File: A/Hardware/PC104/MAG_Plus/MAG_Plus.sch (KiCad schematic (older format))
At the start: 39 parts, among them J1 RPi_GPIO, J9 Conn_01x06_Male, SW1 SW_Push, U1 Payload, U12 PIC16F1847-I_SO, U13 LP38693MP-3.3, U14 LP38693MP-3.3, U15 LP38693MP-5.0, U16 LP38693MP-3.3, U2 ISO1540

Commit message: More PCB Changes
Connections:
- net PIC_3V3: no longer C6.1, R5.1, R6.1, U2.8 (VCC2)
- net PIC_3V3J: now also C6.1, R5.1, R6.1, U2.8 (VCC2)
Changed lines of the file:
@@
 PIC_SDA
 Text GLabel 2050 5200 1    50   Input ~ 0
-PIC_3V3
+PIC_3V3J
 $Comp
 L Device:R R6
@@
 PIC_SCL
 Text GLabel 2300 5200 1    50   Input ~ 0
-PIC_3V3
+PIC_3V3J
 Text GLabel 4900 4600 2    50   Input ~ 0
-PIC_3V3
+PIC_3V3J
 Text GLabel 4900 4800 2    50   Input ~ 0
 PIC_SCL
@@
 SAT_3V3
 Text GLabel 5750 5600 1    50   Input ~ 0
-PIC_3V3
+PIC_3V3J
 Text GLabel 5250 5900 3    50   Input ~ 0
 GND

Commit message: PCB update
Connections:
- net MAG_EN: now also J1.29 (GPIO05); no longer J1.15 (GPIO22)
- net FOD_DPL: now reaches J1.11 (GPIO17)
- new net FOD_CC: J1.15 (GPIO22)
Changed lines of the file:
@@
 Text GLabel 4500 6600 0    50   Input ~ 0
 FOD_EN
-Text GLabel 7600 2100 0    50   Input ~ 0
+Text GLabel 7600 2800 0    50   Input ~ 0
 MAG_EN
 Text GLabel 3000 6600 0    50   Input ~ 0
@@
 Text Notes 7350 7500 0    79   ~ 0
 Raspberry Pi & PIC 16
+Text GLabel 7600 2100 0    50   Input ~ 0
+FOD_CC
+Text GLabel 7600 1900 0    50   Input ~ 0
+FOD_DPL
 $EndSCHEMATC

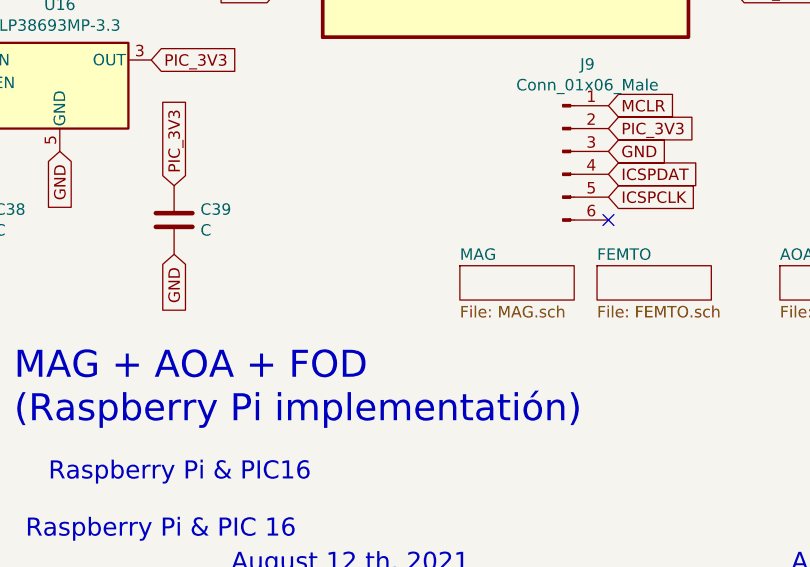
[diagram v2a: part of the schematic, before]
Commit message: add langmuir probe
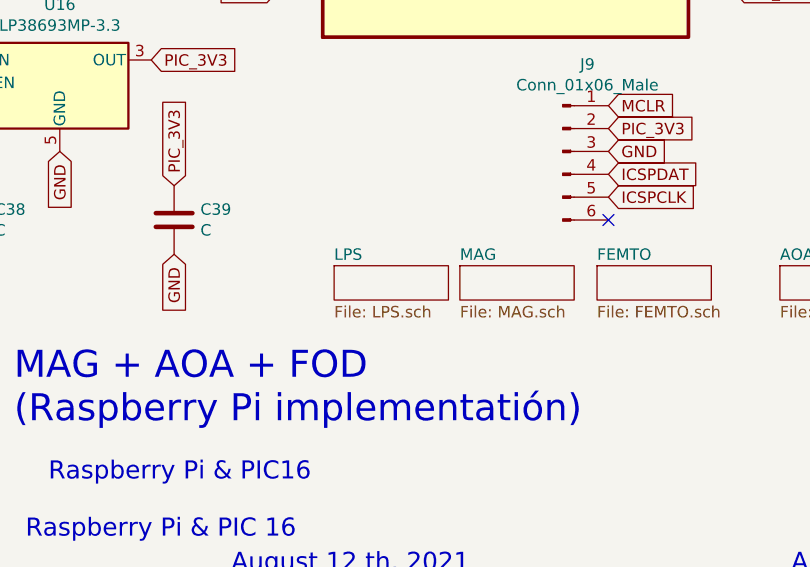
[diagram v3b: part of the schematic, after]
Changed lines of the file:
@@
 $Descr A4 11693 8268
 encoding utf-8
-Sheet 1 4
+Sheet 1 5
 Title ""
 Date ""
@@
 Text GLabel 7600 1900 0    50   Input ~ 0
 FOD_DPL
+$Sheet
+S 8700 6300 500  150
+U 612008B4
+F0 "LPS" 50
+F1 "LPS.sch" 50
+$EndSheet
 $EndSCHEMATC

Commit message: Update PCBs
New version of PCBs
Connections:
- net FOD_STS: now reaches J1.7 (GPIO04_GCLK)
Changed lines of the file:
@@
 F1 "LPS.sch" 50
 $EndSheet
+Text GLabel 7600 1700 0    50   Input ~ 0
+FOD_STS
 $EndSCHEMATC

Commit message: minor changes
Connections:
- net GND: now also U1.81 (29-GND), U1.82 (GND-30), U1.84 (GND-32)
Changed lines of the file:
@@
 Text GLabel 7600 1700 0    50   Input ~ 0
 FOD_STS
+Text GLabel 3950 2600 0    50   Input ~ 0
+GND
+Text GLabel 5500 2600 2    50   Input ~ 0
+GND
+Text GLabel 5500 2700 2    50   Input ~ 0
+GND
 $EndSCHEMATC
